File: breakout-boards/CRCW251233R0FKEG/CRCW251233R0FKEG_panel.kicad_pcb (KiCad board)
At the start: 2 copper layers, 89.7 x 60.8 mm, 64 parts, among them J1 Conn_01x12, J2 Conn_01x12

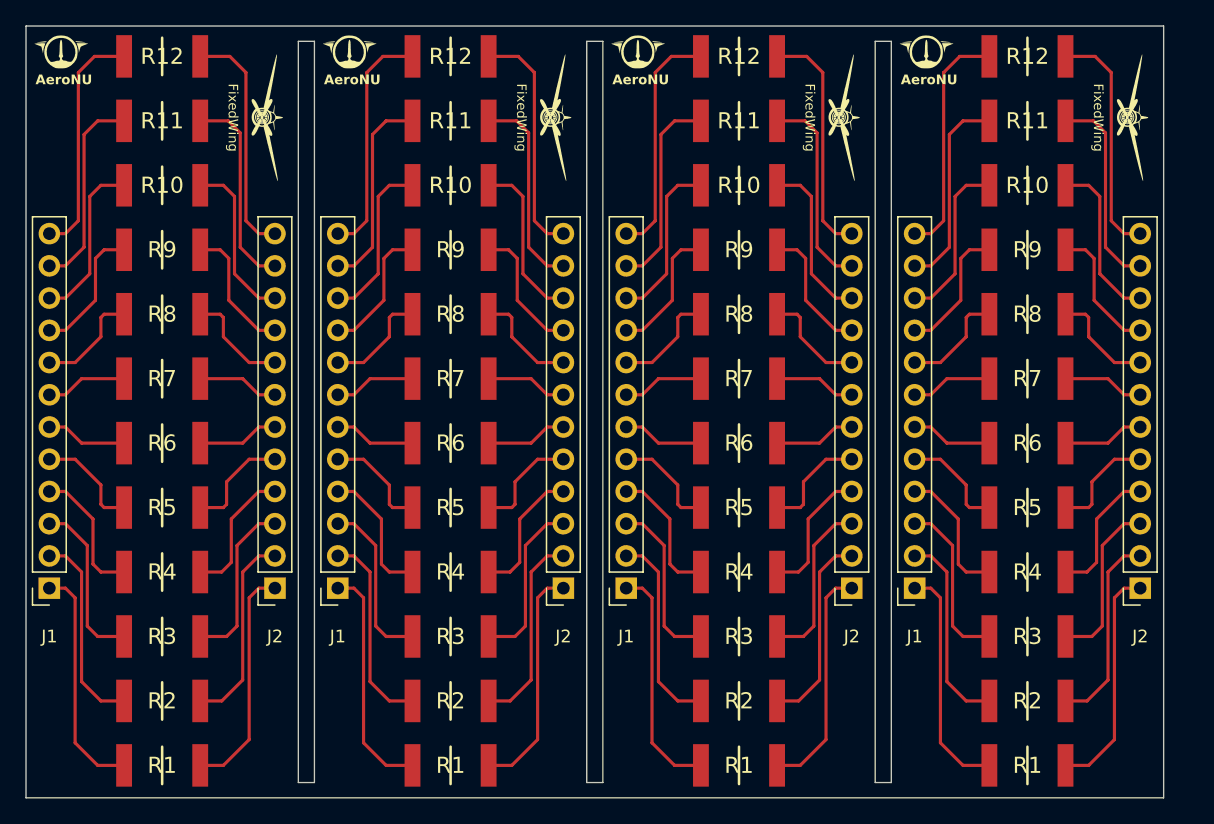
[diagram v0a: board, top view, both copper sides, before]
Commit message: feat: add fillets to all boards
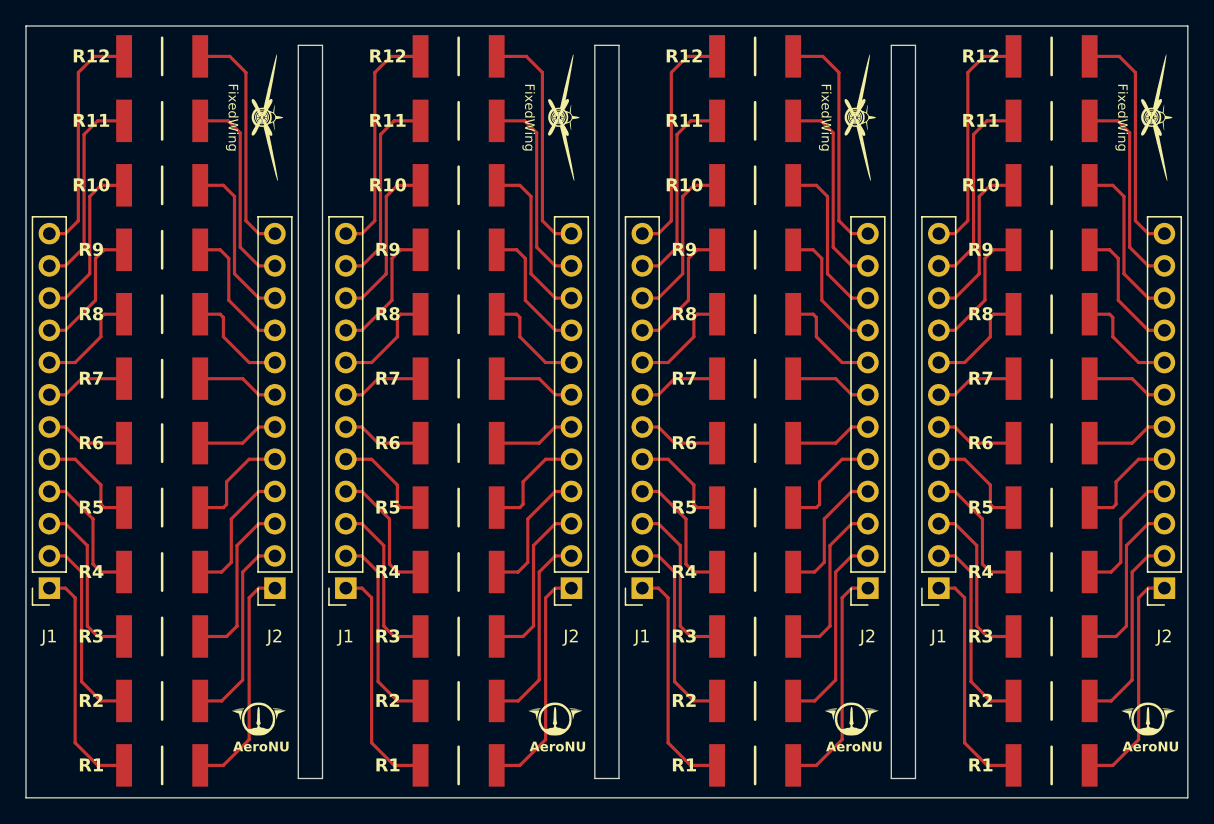
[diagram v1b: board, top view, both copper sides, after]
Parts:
- removed the AeroNU at (173.5, 64.6)
- removed the AeroNU at (150.8, 64.6)
- removed the AeroNU at (196.3, 64.6)
- removed the FixedWing at (212.0, 67.1)
- removed the FixedWing at (166.5, 67.1)
- removed the FixedWing at (189.2, 67.1)
- removed the J1 at (172.5, 104.1)
- removed the J1 at (149.7, 104.1)
- removed the J1 at (195.2, 104.1)
- removed the J2 at (213.0, 104.1)
- removed the J2 at (190.2, 104.1)
- removed the J2 at (167.5, 104.1)
- removed the R1 at (158.6, 118.1)
- removed the R1 at (181.4, 118.1)
- removed the R1 at (204.1, 118.1)
- removed the R10 at (158.6, 72.4)
- removed the R10 at (181.4, 72.4)
- removed the R10 at (204.1, 72.4)
- removed the R11 at (204.1, 67.3)
- removed the R11 at (158.6, 67.3)
- removed the R11 at (181.4, 67.3)
- removed the R12 at (158.6, 62.2)
- removed the R12 at (204.1, 62.2)
- removed the R12 at (181.4, 62.2)
- removed the R2 at (204.1, 113.0)
- removed the R2 at (158.6, 113.0)
- removed the R2 at (181.4, 113.0)
- removed the R3 at (158.6, 108.0)
- removed the R3 at (181.4, 108.0)
- removed the R3 at (204.1, 108.0)
- removed the R4 at (158.6, 102.9)
- removed the R4 at (181.4, 102.9)
- removed the R4 at (204.1, 102.9)
- removed the R5 at (158.6, 97.8)
- removed the R5 at (204.1, 97.8)
- removed the R5 at (181.4, 97.8)
- removed the R6 at (158.6, 92.7)
- removed the R6 at (204.1, 92.7)
- removed the R6 at (181.4, 92.7)
- removed the R7 at (181.4, 87.6)
- removed the R7 at (158.6, 87.6)
- removed the R7 at (204.1, 87.6)
- removed the R8 at (204.1, 82.5)
- removed the R8 at (158.6, 82.5)
- removed the R8 at (181.4, 82.5)
- removed the R9 at (181.4, 77.5)
- removed the R9 at (204.1, 77.5)
- removed the R9 at (158.6, 77.5)
- added AeroNU: LOGO, FixedWing:AeroNU - Logo (Smol), F.Cu at (167.0, 117.2)
- added AeroNU: LOGO, FixedWing:AeroNU - Logo (Smol), F.Cu at (213.7, 117.2)
- added AeroNU: LOGO, FixedWing:AeroNU - Logo (Smol), F.Cu at (190.4, 117.2)
- added FixedWing: LOGO, FixedWing Symbols:FixedWing - Logo (Smol), F.Cu at (167.1, 67.1)
- added FixedWing: LOGO, FixedWing Symbols:FixedWing - Logo (Smol), F.Cu at (213.9, 67.1)
- added FixedWing: LOGO, FixedWing Symbols:FixedWing - Logo (Smol), F.Cu at (190.5, 67.1)
- added J1: Conn_01x12, Connector_PinSocket_2.54mm:PinSocket_1x12_P2.54mm_Vertical, F.Cu at (173.7, 104.1)
- added J1: Conn_01x12, Connector_PinSocket_2.54mm:PinSocket_1x12_P2.54mm_Vertical, F.Cu at (150.4, 104.1)
- added J1: Conn_01x12, Connector_PinSocket_2.54mm:PinSocket_1x12_P2.54mm_Vertical, F.Cu at (197.1, 104.1)
- added J2: Conn_01x12, Connector_PinSocket_2.54mm:PinSocket_1x12_P2.54mm_Vertical, F.Cu at (168.1, 104.1)
- added J2: Conn_01x12, Connector_PinSocket_2.54mm:PinSocket_1x12_P2.54mm_Vertical, F.Cu at (191.5, 104.1)
- added J2: Conn_01x12, Connector_PinSocket_2.54mm:PinSocket_1x12_P2.54mm_Vertical, F.Cu at (214.9, 104.1)
- added R1: 33Ω, FixedWing Symbols:RESC6332X70N, F.Cu at (206.0, 118.1)
- added R1: 33Ω, FixedWing Symbols:RESC6332X70N, F.Cu at (182.6, 118.1)
- added R1: 33Ω, FixedWing Symbols:RESC6332X70N, F.Cu at (159.3, 118.1)
- added R10: 33Ω, FixedWing Symbols:RESC6332X70N, F.Cu at (182.6, 72.4)
- added R10: 33Ω, FixedWing Symbols:RESC6332X70N, F.Cu at (206.0, 72.4)
- added R10: 33Ω, FixedWing Symbols:RESC6332X70N, F.Cu at (159.3, 72.4)
- added R11: 33Ω, FixedWing Symbols:RESC6332X70N, F.Cu at (159.3, 67.3)
- added R11: 33Ω, FixedWing Symbols:RESC6332X70N, F.Cu at (206.0, 67.3)
- added R11: 33Ω, FixedWing Symbols:RESC6332X70N, F.Cu at (182.6, 67.3)
- added R12: 33Ω, FixedWing Symbols:RESC6332X70N, F.Cu at (206.0, 62.2)
- added R12: 33Ω, FixedWing Symbols:RESC6332X70N, F.Cu at (182.6, 62.2)
- added R12: 33Ω, FixedWing Symbols:RESC6332X70N, F.Cu at (159.3, 62.2)
- added R2: 33Ω, FixedWing Symbols:RESC6332X70N, F.Cu at (206.0, 113.0)
- added R2: 33Ω, FixedWing Symbols:RESC6332X70N, F.Cu at (182.6, 113.0)
- added R2: 33Ω, FixedWing Symbols:RESC6332X70N, F.Cu at (159.3, 113.0)
- added R3: 33Ω, FixedWing Symbols:RESC6332X70N, F.Cu at (182.6, 108.0)
- added R3: 33Ω, FixedWing Symbols:RESC6332X70N, F.Cu at (206.0, 108.0)
- added R3: 33Ω, FixedWing Symbols:RESC6332X70N, F.Cu at (159.3, 108.0)
- added R4: 33Ω, FixedWing Symbols:RESC6332X70N, F.Cu at (159.3, 102.9)
- added R4: 33Ω, FixedWing Symbols:RESC6332X70N, F.Cu at (206.0, 102.9)
- added R4: 33Ω, FixedWing Symbols:RESC6332X70N, F.Cu at (182.6, 102.9)
- added R5: 33Ω, FixedWing Symbols:RESC6332X70N, F.Cu at (206.0, 97.8)
- added R5: 33Ω, FixedWing Symbols:RESC6332X70N, F.Cu at (159.3, 97.8)
- added R5: 33Ω, FixedWing Symbols:RESC6332X70N, F.Cu at (182.6, 97.8)
- added R6: 33Ω, FixedWing Symbols:RESC6332X70N, F.Cu at (159.3, 92.7)
- added R6: 33Ω, FixedWing Symbols:RESC6332X70N, F.Cu at (206.0, 92.7)
- added R6: 33Ω, FixedWing Symbols:RESC6332X70N, F.Cu at (182.6, 92.7)
- added R7: 33Ω, FixedWing Symbols:RESC6332X70N, F.Cu at (159.3, 87.6)
- added R7: 33Ω, FixedWing Symbols:RESC6332X70N, F.Cu at (182.6, 87.6)
- added R7: 33Ω, FixedWing Symbols:RESC6332X70N, F.Cu at (206.0, 87.6)
- added R8: 33Ω, FixedWing Symbols:RESC6332X70N, F.Cu at (182.6, 82.5)
- added R8: 33Ω, FixedWing Symbols:RESC6332X70N, F.Cu at (159.3, 82.5)
- added R8: 33Ω, FixedWing Symbols:RESC6332X70N, F.Cu at (206.0, 82.5)
- added R9: 33Ω, FixedWing Symbols:RESC6332X70N, F.Cu at (159.3, 77.5)
- added R9: 33Ω, FixedWing Symbols:RESC6332X70N, F.Cu at (206.0, 77.5)
- added R9: 33Ω, FixedWing Symbols:RESC6332X70N, F.Cu at (182.6, 77.5)
- moved AeroNU 54.8 mm to (143.6, 117.2)
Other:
- board size 89.7 x 60.8 mm -> 91.6 x 60.8 mm
